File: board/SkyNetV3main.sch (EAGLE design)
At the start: 67 parts, among them IC1 HC_05, IC2 RF4463PRO, IC3 LPC1768, IC4 BCX17, IC5 TPS63001, IC6 MCP73871-2CCI/ML, Q1 32.768KHz, Q2 12MHz, Q3 IRLM6402, Q4 BSS138, X1 BAT

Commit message: new layout
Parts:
- removed C14: 100n, rcl:C-EUC0603
- removed JP1: MEASURE, jumper:JP1Q
- removed JP2: DEBUG, pinhead:PINHD-1X5
- removed JP4: PERIPH, microbuilder:HEADER-2X51.27MM
- removed JP5: PROG, jumper:JP1Q
- removed LED1: STATUS, skynet_other:RGB-LED
- removed OK1, OK2, OK3: PC3H7, skynet_other:PC3H7
- removed R7, R8: 91, rcl:R-EU_R0603
- removed S3: INPUT, skynet_other:PT645VERT
- added D1: 3v3, diode:ZENER-DIODESOT23
- added LED2: RGBLED5050, adafruit:RGBLED5050
- added S1: INPUT, switch-ck:PTS645SSMTR
- added SJ1: (no value), jumper:SJ
- added SJ2: PROG, jumper:SJ
- added U$2: (no value), skynet_other:PIN-HEAD-1X3
- C12, C13: value 100n -> 100u; device rcl:C-EUC0603 -> microbuilder:CAP_TANTALUMC/6032_WAVE
- C4, C5: value 33p -> 18p
- Q1: device crystal-2:CRYSTALMM20SS -> skynet_other:XTAL2-PAD
- Q2: device microbuilder:CRYSTALSMD -> skynet_other:XTAL4-PAD
- R6: value 91 -> 10k
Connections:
- net BT_AT renamed BT-AT
- net BT_RX renamed BT-RX
- net BT_TX renamed BT-TX
- net RTCX2 renamed N$2
- net SDI renamed RF-SDI
- net SPI0-NIRQ renamed RF-NIRQ
- net SPI0-NSEL renamed RF-NSEL
- net SPI0-SCLK renamed RF-SCLK
- net SPI0-SDN renamed RF-SDN
- net SPI0-SDO renamed RF-SDO
- removed net BT-RST: IC1.RST, IC3.P0[22]/RTS1/TD1
- removed net CHGSEL_H: IC3.P3[25]/MAT0[0]/PWM1[2], IC6.SEL
- removed net CHGSEL_L: IC3.P3[26]/STCLK/MAT0[1]/PWM1[3], IC6.PROG2
- removed net CHG_S1: IC3.P0[10]/TXD2/SDA2/MAT3[0], OK3.COL
- removed net CHG_S2: IC3.P0[11]/RXD2/SCL2/MAT3[1], OK2.COL
- removed net EXT_GPIO0: IC3.P2[3]/PWM1[4]/DCD1/TRACEDATA[2], JP4.6
- removed net EXT_GPIO1: IC3.P2[4]/PWM1[5]/DSR1/TRACEDATA[1], JP4.8
- removed net EXT_PWR: IC3.P2[12]/EINT2/I2STX_WS, OK1.COL
- removed net LED_B: IC3.P2[2]/PWM1[3]/CTS1/TRACEDATA[3], LED1-B.C
- removed net LED_G: IC3.P2[1]/PWM1[2]/RXD1, LED1-G.C
- removed net LED_R: IC3.P2[0]/PWM1[1]/TXD1, LED1-R.C
- removed net PG: IC6./PG, R6.1
- removed net PG-OK: OK1.C, R6.2
- removed net SCL_EXT: IC3.P0[28]/SCL0/USB_SCL, JP4.4
- removed net SDA_EXT: IC3.P0[27]/SDA0/USB_SDA, JP4.2
- removed net SPI2_MISO: IC3.P0[8]/I2STX_WS/MISO1/MAT2[2], JP4.5
- removed net SPI2_MOSI: IC3.P0[9]/I2STX_SDA/MOSI1/MAT2[3], JP4.7
- removed net SPI2_SCK: IC3.P0[7]/I2STX_CLK/SCK1/MAT2[1], JP4.3
- removed net SPI2_SEL: IC3.P0[6]/I2SRX_SDA/SSEL1/MAT2[0], JP4.1
- removed net STAT1: IC6.STAT1/LBO, R8.1
- removed net STAT1-OK: OK3.C, R8.2
- removed net STAT2: IC6.STAT2, R7.1
- removed net STAT2-OK: OK2.C, R7.2
- new net BT-RESET: IC1.RST, IC3.P1[0]/ENET_TXD0
- new net CHG-S1: IC3.P0[10]/TXD2/SDA2/MAT3[0], IC6.STAT1/LBO
- new net CHG-S2: IC3.P0[11]/RXD2/SCL2/MAT3[1], IC6.STAT2
- new net CHGSEL-H: IC3.P0[25]/AD0[2]/I2SRX_SDA/TXD3, IC6.SEL
- new net CHGSEL-L: IC3.P0[26]/AD0[3]/AOUT/RXD3, IC6.PROG2
- new net EXT-PWR: D1.C, IC3.P2[12]/EINT2/I2STX_WS, R6.2
- new net LED-B: IC3.P2[0]/PWM1[1]/TXD1, LED2.BLUE_C
- new net LED-G: IC3.P2[2]/PWM1[3]/CTS1/TRACEDATA[3], LED2.GREEN_C
- new net LED-R: IC3.P2[1]/PWM1[2]/RXD1, LED2.RED_C
- new net SCL-EXT: IC3.P0[28]/SCL0/USB_SCL, U$2.4
- new net SDA-EXT: IC3.P0[27]/SDA0/USB_SDA, U$2.3
- net +3V3: now also C12.+, C13.+, U$2.5; no longer C12.1, C13.1, C14.1, JP2.4, JP4.10
- net +5V: now also R6.1; no longer OK1.A, OK2.A, OK3.A
- net GND: now also C12.-, C13.-, D1.A, S1.S, SJ2.1, U$2.6; no longer C12.2, C13.2, C14.2, JP2.5, JP4.9, JP5.2, OK1.EMI, OK2.EMI, OK3.EMI, S3.S
- net INPUT: now also S1.P; no longer S3.P
- net LED-B-R: now also LED2.BLUE_A; no longer LED1-B.A
- net LED-G-R: now also LED2.GREEN_A; no longer LED1-G.A
- net LED-R-R: now also LED2.RED_A; no longer LED1-R.A
- net OUT2: now also SJ1.1; no longer JP1.1
- net PROG: now also SJ2.2; no longer JP5.1
- net RX: now also U$2.1; no longer JP2.1
- net TX: now also U$2.2; no longer JP2.3
- net VCC: now also SJ1.2; no longer JP1.2
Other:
- note added: "tantal fehlen"
- moved on the sheet: C1, C10, C15, C2, C3, C4, C5, C9, IC1, IC2, IC3, IC4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

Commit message: another layout try, looks much better now
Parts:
- removed U$2: (no value), skynet_other:PIN-HEAD-1X3
- added JP4: (no value), skynet_other:PIN-HEAD-1X3
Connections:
- net N$2 renamed RTCX2
- net +3V3: now also JP4.5; no longer U$2.5
- net AD-PWR: now also IC3.P1[0]/ENET_TXD0; no longer IC3.P1[29]/MCOB2/PCAP1[1]/MAT0[1]
- net BT-AT: now also IC3.P2[13]/EINT3/I2STX_SDA; no longer IC3.P2[5]/PWM1[6]/DTR1/TRACEDATA[0]
- net BT-RESET: now also IC3.P0[11]/RXD2/SCL2/MAT3[1]; no longer IC3.P1[0]/ENET_TXD0
- net CHG-S1: now also IC3.P0[22]/RTS1/TD1; no longer IC3.P0[10]/TXD2/SDA2/MAT3[0]
- net CHG-S2: now also IC3.P0[21]/RI1/RD1; no longer IC3.P0[11]/RXD2/SCL2/MAT3[1]
- net CHGSEL-H: now also IC3.P2[3]/PWM1[4]/DCD1/TRACEDATA[2]; no longer IC3.P0[25]/AD0[2]/I2SRX_SDA/TXD3
- net CHGSEL-L: now also IC3.P2[4]/PWM1[5]/DSR1/TRACEDATA[1]; no longer IC3.P0[26]/AD0[3]/AOUT/RXD3
- net GND: now also JP4.6; no longer U$2.6
- net RF-SDN: now also IC3.P2[8]/TD2/TXD2/ENET_MDC; no longer IC3.P0[21]/RI1/RD1
- net RX: now also JP4.2; no longer U$2.1
- net SCL-EXT: now also JP4.4; no longer U$2.4
- net SDA-EXT: now also JP4.3; no longer U$2.3
- net TX: now also JP4.1; no longer U$2.2
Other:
- note removed: "tantal fehlen"

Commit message: layout improvements
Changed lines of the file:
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@@
 <segment>
 <pinref part="IC6" gate="A" pin="STAT1/LBO"/>
-<wire x1="60.96" y1="93.98" x2="40.64" y2="93.98" width="0.1524" layer="91"/>
-<wire x1="40.64" y1="93.98" x2="40.64" y2="124.46" width="0.1524" layer="91"/>
-<wire x1="88.9" y1="124.46" x2="40.64" y2="124.46" width="0.1524" layer="91"/>
-<label x="88.9" y="124.46" size="1.778" layer="95" xref="yes"/>
+<wire x1="60.96" y1="93.98" x2="55.88" y2="93.98" width="0.1524" layer="91"/>
+<label x="55.88" y="93.98" size="1.27" layer="95" rot="R180" xref="yes"/>
 </segment>
 </net>
@@
 <segment>
 <pinref part="IC6" gate="A" pin="STAT2"/>
-<wire x1="60.96" y1="96.52" x2="38.1" y2="96.52" width="0.1524" layer="91"/>
-<wire x1="38.1" y1="96.52" x2="38.1" y2="129.54" width="0.1524" layer="91"/>
-<label x="88.9" y="129.54" size="1.778" layer="95" rot="MR180" xref="yes"/>
-<wire x1="38.1" y1="129.54" x2="88.9" y2="129.54" width="0.1524" layer="91"/>
+<wire x1="60.96" y1="96.52" x2="55.88" y2="96.52" width="0.1524" layer="91"/>
+<label x="55.88" y="96.52" size="1.27" layer="95" rot="MR0" xref="yes"/>
 </segment>
 </net>

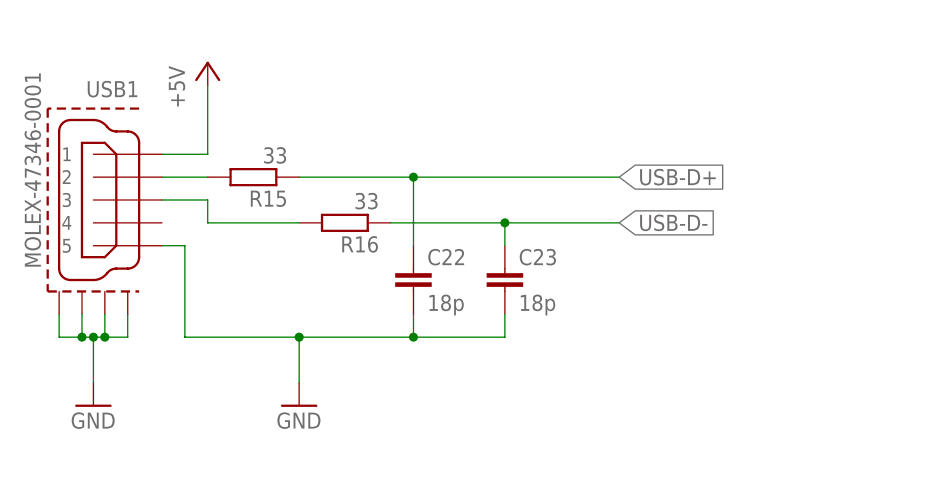
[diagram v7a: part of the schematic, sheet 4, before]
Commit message: corrected USB connector in layout+schematics
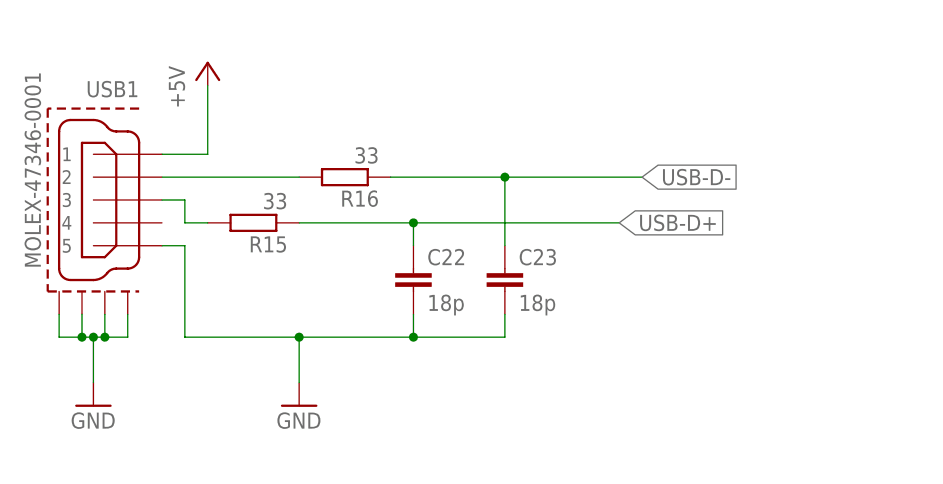
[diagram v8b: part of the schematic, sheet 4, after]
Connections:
- removed net USB-D+_IN: R15.2, USB1.2
- removed net USB-D-_IN: R16.2, USB1.3
- new net N$2: R16.2, USB1.2
- new net N$3: R15.2, USB1.3
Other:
- moved on the sheet: R15, R16
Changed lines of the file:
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@@
 <instance part="USB1" gate="G$1" x="25.4" y="149.86" rot="MR0"/>
 <instance part="P+1" gate="1" x="35.56" y="165.1"/>
-<instance part="R15" gate="G$1" x="40.64" y="152.4" rot="R180"/>
-<instance part="R16" gate="G$1" x="50.8" y="147.32" rot="R180"/>
+<instance part="R15" gate="G$1" x="40.64" y="147.32" rot="R180"/>
+<instance part="R16" gate="G$1" x="50.8" y="152.4" rot="R180"/>
 <instance part="C22" gate="G$1" x="58.42" y="142.24"/>
 <instance part="C23" gate="G$1" x="68.58" y="142.24"/>
@@
 <segment>
 <pinref part="R15" gate="G$1" pin="1"/>
-<wire x1="45.72" y1="152.4" x2="58.42" y2="152.4" width="0.1524" layer="91"/>
+<wire x1="45.72" y1="147.32" x2="58.42" y2="147.32" width="0.1524" layer="91"/>
 <pinref part="C22" gate="G$1" pin="1"/>
-<wire x1="58.42" y1="152.4" x2="81.28" y2="152.4" width="0.1524" layer="91"/>
-<wire x1="58.42" y1="144.78" x2="58.42" y2="152.4" width="0.1524" layer="91"/>
-<junction x="58.42" y="152.4"/>
-<label x="81.28" y="152.4" size="1.778" layer="95" xref="yes"/>
+<wire x1="58.42" y1="147.32" x2="81.28" y2="147.32" width="0.1524" layer="91"/>
+<wire x1="58.42" y1="144.78" x2="58.42" y2="147.32" width="0.1524" layer="91"/>
+<junction x="58.42" y="147.32"/>
+<label x="81.28" y="147.32" size="1.778" layer="95" xref="yes"/>
 </segment>
 </net>
@@
 <segment>
 <pinref part="R16" gate="G$1" pin="1"/>
-<wire x1="55.88" y1="147.32" x2="68.58" y2="147.32" width="0.1524" layer="91"/>
+<wire x1="55.88" y1="152.4" x2="68.58" y2="152.4" width="0.1524" layer="91"/>
 <pinref part="C23" gate="G$1" pin="1"/>
-<wire x1="68.58" y1="147.32" x2="81.28" y2="147.32" width="0.1524" layer="91"/>
-<wire x1="68.58" y1="144.78" x2="68.58" y2="147.32" width="0.1524" layer="91"/>
-<junction x="68.58" y="147.32"/>
-<label x="81.28" y="147.32" size="1.778" layer="95" xref="yes"/>
-</segment>
-</net>
-<net name="USB-D+_IN" class="0">
-<segment>
-<pinref part="USB1" gate="G$1" pin="2"/>
-<pinref part="R15" gate="G$1" pin="2"/>
-<wire x1="30.48" y1="152.4" x2="35.56" y2="152.4" width="0.1524" layer="91"/>
-</segment>
-</net>
-<net name="USB-D-_IN" class="0">
-<segment>
-<pinref part="USB1" gate="G$1" pin="3"/>
-<wire x1="30.48" y1="149.86" x2="35.56" y2="149.86" width="0.1524" layer="91"/>
-<wire x1="35.56" y1="149.86" x2="35.56" y2="147.32" width="0.1524" layer="91"/>
-<pinref part="R16" gate="G$1" pin="2"/>
-<wire x1="35.56" y1="147.32" x2="45.72" y2="147.32" width="0.1524" layer="91"/>
+<wire x1="68.58" y1="152.4" x2="83.82" y2="152.4" width="0.1524" layer="91"/>
+<wire x1="68.58" y1="144.78" x2="68.58" y2="152.4" width="0.1524" layer="91"/>
+<junction x="68.58" y="152.4"/>
+<label x="83.82" y="152.4" size="1.778" layer="95" xref="yes"/>
 </segment>
 </net>
@@
 </segment>
 </net>
+<net name="N$2" class="0">
+<segment>
+<pinref part="USB1" gate="G$1" pin="2"/>
+<pinref part="R16" gate="G$1" pin="2"/>
+<wire x1="30.48" y1="152.4" x2="45.72" y2="152.4" width="0.1524" layer="91"/>
+</segment>
+</net>
+<net name="N$3" class="0">
+<segment>
+<pinref part="R15" gate="G$1" pin="2"/>
+<wire x1="35.56" y1="147.32" x2="33.02" y2="147.32" width="0.1524" layer="91"/>
+<wire x1="33.02" y1="147.32" x2="33.02" y2="149.86" width="0.1524" layer="91"/>
+<pinref part="USB1" gate="G$1" pin="3"/>
+<wire x1="33.02" y1="149.86" x2="30.48" y2="149.86" width="0.1524" layer="91"/>
+</segment>
+</net>
